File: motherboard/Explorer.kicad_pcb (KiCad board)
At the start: 2 copper layers, 80 x 55 mm, 72 parts, among them J1 USB_B_Micro, J2 EHZ, J3 EHN, J4 EHE, J5 locked, J6 RS232, SW1 POWER, SW2 BAUDRATE, U1 ADS1262IPWR, U2 AMS1117-3.3, U4 locked, Y1 8MHz

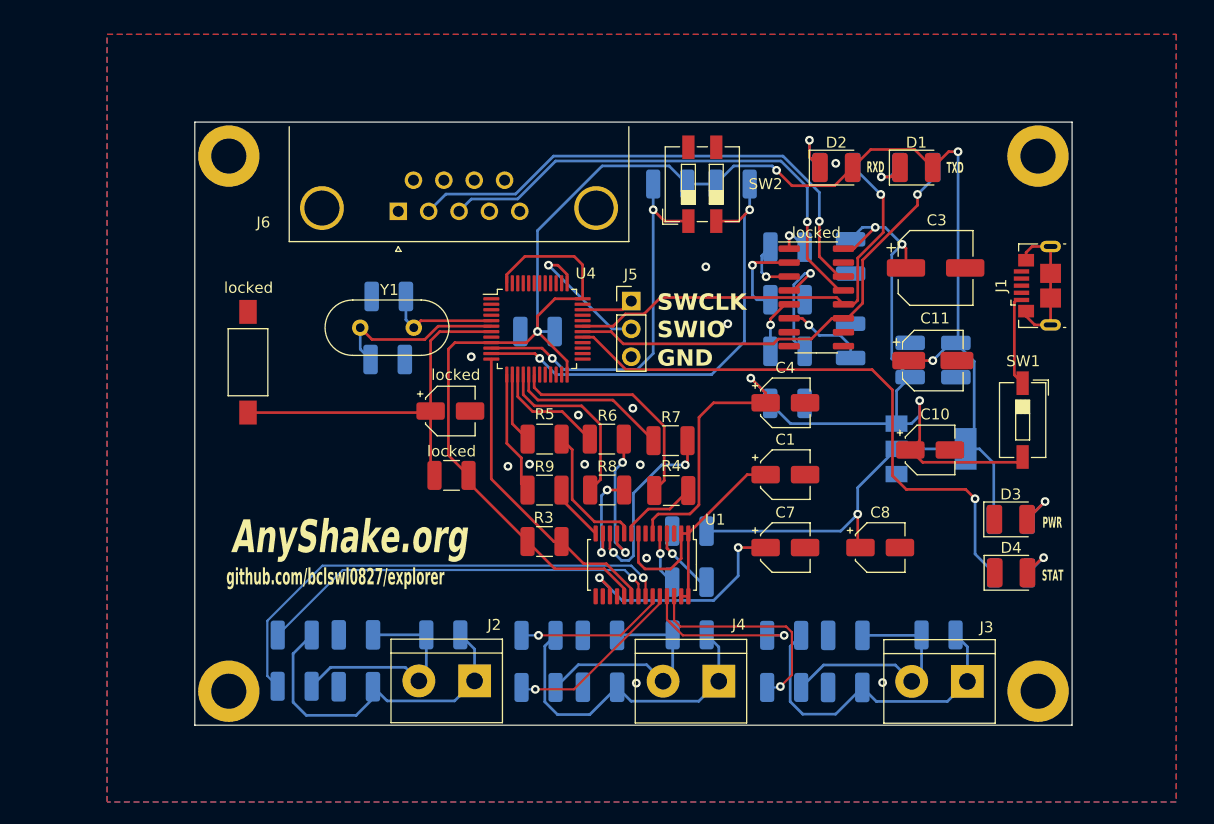
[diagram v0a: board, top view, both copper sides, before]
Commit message: Change MCU to ESP-12F
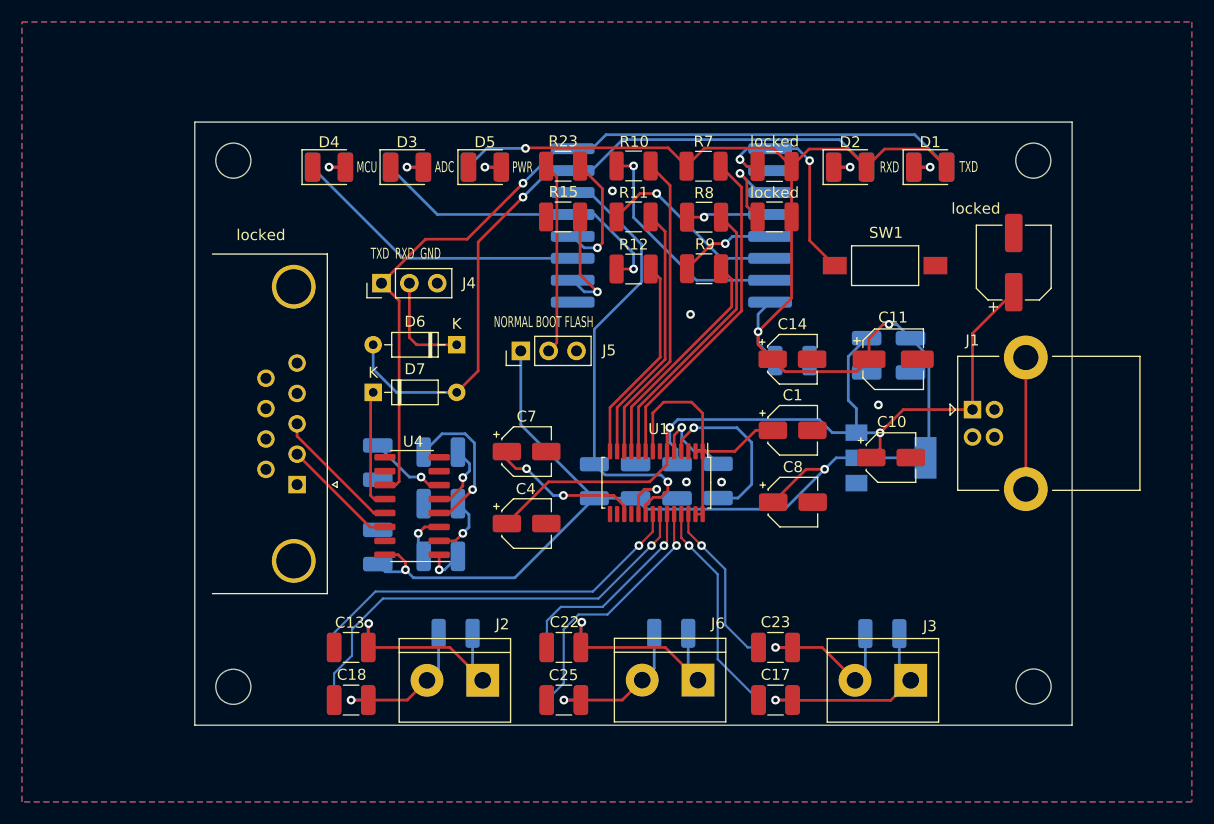
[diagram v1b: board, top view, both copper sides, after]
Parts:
- removed the C19 at (127.4, 86.0)
- removed the C23 at (127.3, 91.7)
- removed the R2 at (158.8, 75.7)
- removed REF** (x4): MountingHole_3.2mm_M3_DIN965_Pad, MountingHole:MountingHole_3.2mm_M3_DIN965_Pad
- removed SW2: BAUDRATE, Button_Switch_SMD:SW_DIP_SPSTx02_Slide_6.7x6.64mm_W6.73mm_P2.54mm_LowProfile_JPin
- removed the U4 at (140.9, 89.0)
- removed Y1: 8MHz, Crystal:Crystal_HC49-U_Vertical
- removed the locked at (133.0, 96.4)
- removed the locked at (133.2, 102.3)
- removed the locked at (114.6, 92.0)
- added C15: 0.1uF, Capacitor_SMD:C_1210_3225Metric_Pad1.33x2.70mm_HandSolder, B.Cu at (164.2, 91.8)
- added D3: ADC_STATE, LED_SMD:LED_1210_3225Metric_Pad1.42x2.65mm_HandSolder, F.Cu at (129.1, 74.2)
- added D6: 1N4148, Diode_THT:D_DO-35_SOD27_P7.62mm_Horizontal, F.Cu at (133.6, 90.4)
- added D7: 1N4148, Diode_THT:D_DO-35_SOD27_P7.62mm_Horizontal, F.Cu at (126.0, 94.7)
- added H1: MountingHole, MountingHole:MountingHole_3.2mm_M3, F.Cu at (113.3, 73.6)
- added H2: MountingHole, MountingHole:MountingHole_3.2mm_M3, F.Cu at (113.3, 121.6)
- added H3: MountingHole, MountingHole:MountingHole_3.2mm_M3, F.Cu at (186.2, 121.6)
- added H4: MountingHole, MountingHole:MountingHole_3.2mm_M3, F.Cu at (186.2, 73.6)
- added J4: TTL_DEBUG, Connector_PinHeader_2.54mm:PinHeader_1x03_P2.54mm_Vertical, F.Cu at (126.8, 84.8)
- added R15: 10k, Resistor_SMD:R_1210_3225Metric_Pad1.30x2.65mm_HandSolder, F.Cu at (143.3, 78.7)
- added R23: 10k, Resistor_SMD:R_1210_3225Metric_Pad1.30x2.65mm_HandSolder, F.Cu at (143.3, 74.1)
- added locked: locked, Resistor_SMD:R_1210_3225Metric_Pad1.30x2.65mm_HandSolder, F.Cu at (162.6, 78.7)
- added locked: locked, Resistor_SMD:R_1210_3225Metric_Pad1.30x2.65mm_HandSolder, F.Cu at (162.6, 74.1)
- added locked: locked, Explorer_Project:ESP-12F, B.Cu at (153.2, 76.0)
- C13, C18, C22: moved to F.Cu
- C14: value 0.1uF -> 10uF; footprint Capacitor_SMD:C_1210_3225Metric_Pad1.33x2.70mm_HandSolder -> Capacitor_SMD:CP_Elec_4x5.3; moved to F.Cu
- C17: renamed from C16; moved to F.Cu
- C23: renamed from C24; moved to F.Cu
- C25: renamed from C27; moved to F.Cu
- J1: value USB_B_Micro -> USB_B; footprint Connector_USB:USB_Micro-B_GCT_USB3076-30-A -> Connector_USB:USB_B_Lumberg_2411_02_Horizontal
- J5: value locked -> MODE_SEL
- R1: value 10k -> 1k
- R6: renamed from R3; moved to B.Cu
- SW1: value POWER -> RESET; footprint Button_Switch_SMD:SW_DIP_SPSTx01_Slide_6.7x4.1mm_W6.73mm_P2.54mm_LowProfile_JPin -> Button_Switch_SMD:SW_SPST_FSMSM
- moved R2 72.4 mm to (122.0, 74.2)
- moved D4 72.4 mm to (122.0, 74.2)
- moved R3 57.7 mm to (136.2, 74.2)
- moved D5 57.7 mm to (136.2, 74.2)
- moved C16 50.6 mm to (126.4, 108.8), turned to -90 degrees
- moved locked 44.5 mm to (126.4, 101.1), turned to -90 degrees
- moved C19 42.4 mm to (132.2, 109.7)
- moved U4 41.5 mm to (129.6, 105.1), turned to 180 degrees
- moved C21 36.7 mm to (132.2, 104.9), turned to 180 degrees
- moved locked 32.9 mm to (132.2, 100.2), turned to 0 degrees
- moved R7 29.7 mm to (156.1, 74.1)
- moved locked 26.6 mm to (119.1, 103.1), turned to -90 degrees
- moved C4 26.0 mm to (140.0, 106.7)
- moved R10 25.3 mm to (149.8, 74.1)
- moved C7 25.2 mm to (140.0, 100.1)
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- renumbered C15 to C16, C20 to C19, C25 to C21, D3 to D5, J4 to J6, R7 to R10, R8 to R11, R9 to R12, R14 to R16, R16 to R17, R17 to R18, R18 to R19, R11 to R2, R19 to R20, R20 to R21, R21 to R22, R22 to R24, R23 to R25, R10 to R3, R12 to R4, R13 to R5, R4 to R7, R5 to R8, R6 to R9, locked to U4, J6 to locked, C3 to locked, C21 to locked, C26 to locked
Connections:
- net /TTL_TXD renamed /MCU_TXD
- C14 pad 1: GND -> /+3.3v
- C14 pad 2: /+3.3v -> GND
- C16 pad 2: /+5v -> /+3.3v
- J1 pad 1: Net-(J1-VBUS) -> /+5v
- J1 pad 4: unconnected-(J1-ID-Pad4) -> GND
- J1 pad 5: GND -> unconnected-(J1-Shield-Pad5)
- J5 pad 1: /SWIO -> /+3.3v
- J5 pad 2: /SWCLK -> Net-(J5-Pin_2)
- R1 pad 1: /+3.3v -> /ADC_DRDY
- R1 pad 2: /BAUD_BIT0 -> Net-(D3-A)
- R2 pad 1: /LED_STATE -> /MCU_STATE
- R5 pad 2: /TTL_RXD -> /MCU_RXD
- R7 pad 1: /ADC_START -> /+3.3v
- SW1 pad 1: Net-(J1-VBUS) -> GND
- SW1 pad 2: /+5v -> Net-(U3-RST)
- U4 pad 12: /TTL_RXD -> Net-(D7-K)
- U4 pad 16: /+5v -> /+3.3v
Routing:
- net /MCU_RXD: track 0.00 -> 63.9 mm, vias 0 -> 1
- net /LED_STATE: track 54.0 -> 0.00 mm, vias 1 -> 0
- net /BAUD_BIT1: track 43.2 -> 0.00 mm, vias 2 -> 0
- net /TTL_RXD: track 40.8 -> 0.00 mm, vias 1 -> 0
- net /RS_RXD: track 47.5 -> 10.8 mm, vias 1 -> 0
- net /BAUD_BIT0: track 35.3 -> 0.00 mm, vias 2 -> 0
- net Net-(U4-NRST): track 34.3 -> 0.00 mm
- net /MCU_TXD: track 41.2 -> 75.5 mm
- net /RS_TXD: track 45.3 -> 12.0 mm, vias 1 -> 0
- net /MCU_STATE: track 0.00 -> 27.2 mm
- net Net-(U1-START): track 7.22 -> 30.4 mm
- net /ADC_START: track 20.7 -> 0.00 mm
- net Net-(U3-RST): track 0.00 -> 19.8 mm, vias 0 -> 2
- net Net-(J5-Pin_2): track 0.00 -> 17.6 mm
- net /ADC_DRDY: track 11.3 -> 28.4 mm, vias 0 -> 1
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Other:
- board text added: "ADC"
- board text added: "MCU"
- board text added: "NORMAL BOOT FLASH"
- board text added: "TXD RXD GND"
- board text removed: "+---------------------------------------+ | Baudrate Selector | +------+-------+-------+-------+--------+ | | 19200 | 38400 | 57600 | 115200 | +------+-------+-------+-------+--------+ | BIT0 | L | L | H | H | +------+-------+-------+-------+--------+ | BIT1 | L | H | L | H | +------+-------+-------+-------+--------+"
- board text removed: "AnyShake.org"
- board text removed: "GND"
- board text removed: "STAT"
- board text removed: "SWCLK"
- board text removed: "SWIO"
- board text removed: "github.com/bclswl0827/explorer"
